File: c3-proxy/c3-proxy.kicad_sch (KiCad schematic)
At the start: 14 parts, among them J1 J-SAMTEC-TFM-120-X1-XXX-D-RA, J2 SFM-120-02-X-DH, J3 USB_C_Receptacle_USB2.0_16P, J4 Barrel_Jack, U9 IP4234CZ6,125

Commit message: style and logic fixes
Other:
- note added: "not sure the ideal way to connect/route this capacitor"
- moved on the sheet: HW1, HW2, HW3
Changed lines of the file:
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@@
 		)
 	)
+	(text "not sure the ideal way to connect/route this capacitor"
+		(exclude_from_sim no)
+		(at 53.848 244.856 0)
+		(effects
+			(font
+				(size 1.27 1.27)
+			)
+		)
+	)
 	(text "Outside Negitive\nInside Positive"
 		(exclude_from_sim no)
@@
 	)
 	(junction
+		(at 208.28 69.85)
+		(diameter 0)
+		(color 0 0 0 0)
+	)
+	(junction
 		(at 118.11 105.41)
 		(diameter 0)
@@
 	)
 	(junction
-		(at 208.28 69.85)
-		(diameter 0)
-		(color 0 0 0 0)
-	)
-	(junction
 		(at 118.11 82.55)
 		(diameter 0)
@@
 	(wire
 		(pts
-			(xy 208.28 69.85) (xy 118.11 69.85)
+			(xy 118.11 69.85) (xy 208.28 69.85)
 		)
 		(stroke
@@
 	(wire
 		(pts
-			(xy 208.28 69.85) (xy 208.28 154.94)
-		)
-		(stroke
-			(width 0)
-			(type default)
-		)
-	)
-	(wire
-		(pts
 			(xy 284.48 102.87) (xy 280.67 102.87)
 		)
@@
 	(wire
 		(pts
-			(xy 210.82 74.93) (xy 210.82 154.94)
-		)
-		(stroke
-			(width 0)
-			(type default)
-		)
-	)
-	(wire
-		(pts
 			(xy 284.48 80.01) (xy 118.11 80.01)
 		)
@@
 	(wire
 		(pts
+			(xy 208.28 69.85) (xy 284.48 69.85)
+		)
+		(stroke
+			(width 0)
+			(type default)
+		)
+	)
+	(wire
+		(pts
 			(xy 129.54 102.87) (xy 118.11 102.87)
 		)
@@
 	(wire
 		(pts
+			(xy 208.28 69.85) (xy 208.28 154.94)
+		)
+		(stroke
+			(width 0)
+			(type default)
+		)
+	)
+	(wire
+		(pts
 			(xy 288.29 110.49) (xy 284.48 110.49)
 		)
@@
 	(wire
 		(pts
-			(xy 288.29 54.61) (xy 114.3 54.61)
+			(xy 118.11 74.93) (xy 210.82 74.93)
 		)
 		(stroke
@@
 	(wire
 		(pts
-			(xy 288.29 52.07) (xy 114.3 52.07)
+			(xy 288.29 54.61) (xy 114.3 54.61)
 		)
 		(stroke
@@
 	(wire
 		(pts
-			(xy 83.82 194.31) (xy 88.9 194.31)
+			(xy 288.29 52.07) (xy 114.3 52.07)
 		)
 		(stroke
@@
 	(wire
 		(pts
-			(xy 118.11 77.47) (xy 118.11 80.01)
+			(xy 83.82 194.31) (xy 88.9 194.31)
 		)
 		(stroke
@@
 	(wire
 		(pts
-			(xy 223.52 130.81) (xy 114.3 130.81)
+			(xy 118.11 77.47) (xy 118.11 80.01)
 		)
 		(stroke
@@
 	(wire
 		(pts
-			(xy 273.05 100.33) (xy 273.05 97.79)
+			(xy 223.52 130.81) (xy 114.3 130.81)
 		)
 		(stroke
@@
 	(wire
 		(pts
-			(xy 288.29 74.93) (xy 284.48 74.93)
+			(xy 273.05 100.33) (xy 273.05 97.79)
 		)
 		(stroke
@@
 	(wire
 		(pts
-			(xy 210.82 74.93) (xy 118.11 74.93)
+			(xy 288.29 74.93) (xy 284.48 74.93)
 		)
 		(stroke
@@
 	(wire
 		(pts
-			(xy 284.48 74.93) (xy 210.82 74.93)
-		)
-		(stroke
-			(width 0)
-			(type default)
-		)
-	)
-	(wire
-		(pts
 			(xy 80.01 166.37) (xy 80.01 163.83)
 		)
@@
 	(wire
 		(pts
+			(xy 210.82 74.93) (xy 284.48 74.93)
+		)
+		(stroke
+			(width 0)
+			(type default)
+		)
+	)
+	(wire
+		(pts
 			(xy 288.29 77.47) (xy 284.48 77.47)
 		)
@@
 	(wire
 		(pts
-			(xy 284.48 69.85) (xy 208.28 69.85)
-		)
-		(stroke
-			(width 0)
-			(type default)
-		)
-	)
-	(wire
-		(pts
 			(xy 288.29 92.71) (xy 284.48 92.71)
 		)
@@
 	(wire
 		(pts
+			(xy 210.82 74.93) (xy 210.82 154.94)
+		)
+		(stroke
+			(width 0)
+			(type default)
+		)
+	)
+	(wire
+		(pts
 			(xy 118.11 107.95) (xy 118.11 110.49)
 		)
@@
 	(symbol
 		(lib_id "oresat_stuff:M1.6_Mounting_Hole")
-		(at 340.36 184.15 0)
+		(at 360.68 157.48 0)
 		(unit 1)
 		(body_style 1)
@@
 		(fields_autoplaced yes)
 		(property "Reference" "HW1"
-			(at 342.9 182.8799 0)
+			(at 363.22 156.2099 0)
 			(show_name no)
 			(do_not_autoplace no)
@@
 		)
 		(property "Value" "M1.6_Mounting_Hole"
-			(at 342.9 185.4199 0)
+			(at 363.22 158.7499 0)
 			(show_name no)
 			(do_not_autoplace no)
@@
 		)
 		(property "Footprint" "oresat-misc:M1.6 Mounting Hole"
-			(at 340.36 191.77 0)
+			(at 360.68 165.1 0)
 			(hide yes)
 			(show_name no)
@@
 		)
 		(property "Datasheet" ""
-			(at 340.36 184.15 0)
+			(at 360.68 157.48 0)
 			(hide yes)
 			(show_name no)
@@
 		)
 		(property "Description" ""
-			(at 340.36 184.15 0)
+			(at 360.68 157.48 0)
 			(hide yes)
 			(show_name no)
@@
 	(symbol
 		(lib_id "oresat_stuff:M1.6_Mounting_Hole")
-		(at 340.36 193.04 0)
+		(at 360.68 166.37 0)
 		(unit 1)
 		(body_style 1)
@@
 		(fields_autoplaced yes)
 		(property "Reference" "HW2"
-			(at 342.9 191.7699 0)
+			(at 363.22 165.0999 0)
 			(show_name no)
 			(do_not_autoplace no)
@@
 		)
 		(property "Value" "M1.6_Mounting_Hole"
-			(at 342.9 194.3099 0)
+			(at 363.22 167.6399 0)
 			(show_name no)
 			(do_not_autoplace no)
@@
 		)
 		(property "Footprint" "oresat-misc:M1.6 Mounting Hole"
-			(at 340.36 200.66 0)
+			(at 360.68 173.99 0)
 			(hide yes)
 			(show_name no)
@@
 		)
 		(property "Datasheet" ""
-			(at 340.36 193.04 0)
+			(at 360.68 166.37 0)
 			(hide yes)
 			(show_name no)
@@
 		)
 		(property "Description" ""
-			(at 340.36 193.04 0)
+			(at 360.68 166.37 0)
 			(hide yes)
 			(show_name no)
@@
 	(symbol
 		(lib_id "oresat_stuff:M1.6_Mounting_Hole")
-		(at 340.36 201.93 0)
+		(at 360.68 175.26 0)
 		(unit 1)
 		(body_style 1)
@@
 		(fields_autoplaced yes)
 		(property "Reference" "HW3"
-			(at 342.9 200.6599 0)
+			(at 363.22 173.9899 0)
 			(show_name no)
 			(do_not_autoplace no)
@@
 		)
 		(property "Value" "M1.6_Mounting_Hole"
-			(at 342.9 203.1999 0)
+			(at 363.22 176.5299 0)
 			(show_name no)
 			(do_not_autoplace no)
@@
 		)
 		(property "Footprint" "oresat-misc:M1.6 Mounting Hole"
-			(at 340.36 209.55 0)
+			(at 360.68 182.88 0)
 			(hide yes)
 			(show_name no)
@@
 		)
 		(property "Datasheet" ""
-			(at 340.36 201.93 0)
+			(at 360.68 175.26 0)
 			(hide yes)
 			(show_name no)
@@
 		)
 		(property "Description" ""
-			(at 340.36 201.93 0)
+			(at 360.68 175.26 0)
 			(hide yes)
 			(show_name no)
@@
 		)
 		(pin "OPD_SCL" input
-			(at 210.82 154.94 90)
+			(at 208.28 154.94 90)
 			(effects
 				(font
@@
 		)
 		(pin "OPD_PWR" input
-			(at 208.28 154.94 90)
+			(at 210.82 154.94 90)
 			(effects
 				(font

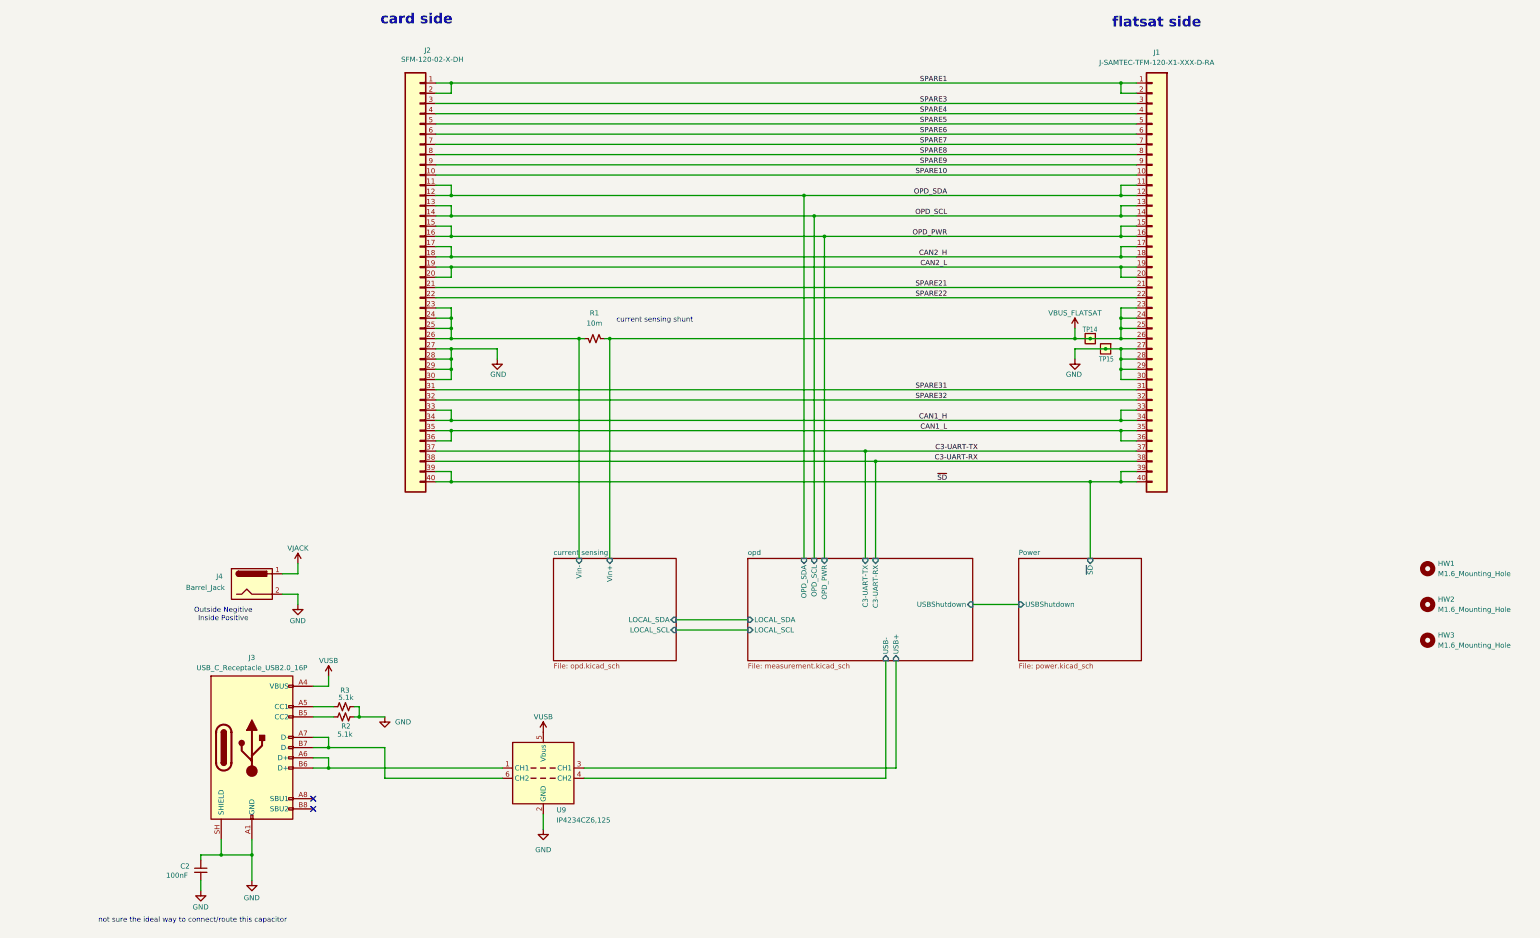
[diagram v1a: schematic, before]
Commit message: final layout and schematic touch ups
killed buzzer
deleted old folder
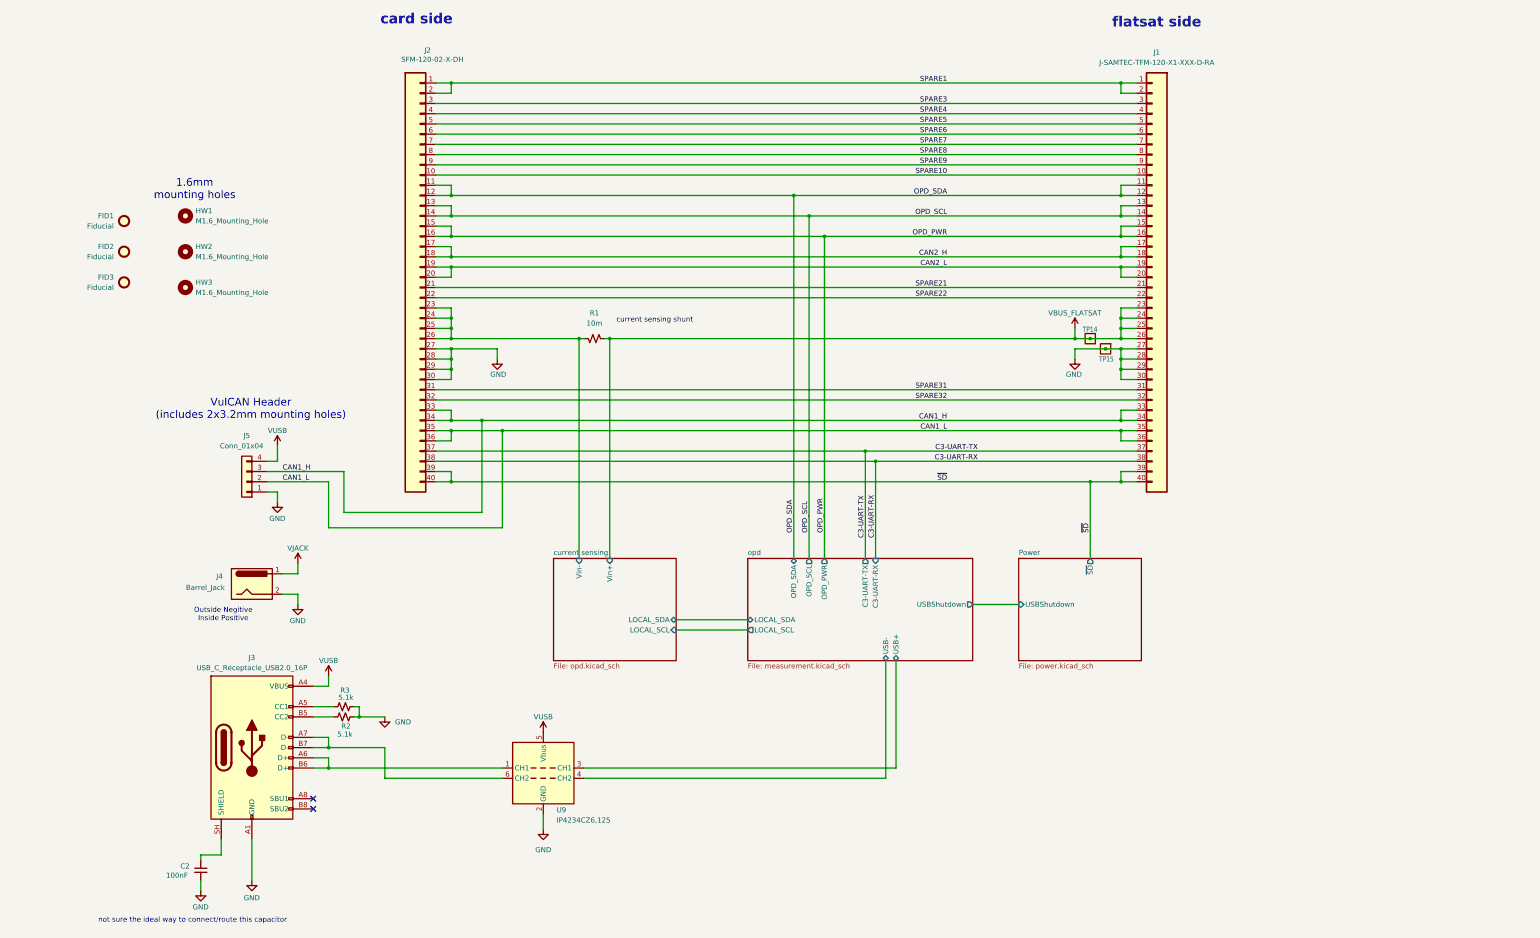
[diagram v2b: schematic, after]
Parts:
- added FID1, FID2, FID3: Fiducial, Fiducial:Fiducial_0.5mm_Mask1mm, symbol Mechanical:Fiducial
- added J5: Conn_01x04, Connector_PinHeader_2.54mm:PinHeader_1x04_P2.54mm_Vertical, symbol Connector_Generic:Conn_01x04
- C2: DIST (none) -> DigiKey; DPN (none) -> 399-6856-1-ND; MFR (none) -> KEMET; MPN (none) -> C0603C104K5RACAUTO
- J1: DIST (none) -> DigiKey; DPN (none) -> SAM10145-ND; MFR (none) -> Samtec Inc.; MPN (none) -> TFM-120-01-L-D-RA
- J2: DIST (none) -> DigiKey; DPN (none) -> SAM11706-ND; MFR (none) -> Samtec Inc.; MPN (none) -> SFM-120-01-S-D-LC
- J3: DIST (none) -> DigiKey; DPN (none) -> 2073-USB4105-GF-ACT-ND; MFR (none) -> GCT; MPN (none) -> USB4105-GF-A
- J4: DIST (none) -> DigiKey; DPN (none) -> CP-002A-ND; MFR (none) -> Category Connectors, Interconnects, Barrel Connectors, Powe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; MPN (none) -> PJ-002A
- R1: DIST (none) -> DigiKey; DPN (none) -> 696-1374-1-ND; MFR (none) -> Riedon; MPN (none) -> CSR1206-0R01F1
- R2, R3: DIST (none) -> DigiKey; DPN (none) -> RMCF0603FT5K10CT-ND; MFR (none) -> Stackpole Electronics; MPN (none) -> RMCF0603FT5K10
- U9: DIST (none) -> DigiKey
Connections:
- net CAN1_H: now also J5.3 (Pin_3)
- net CAN1_L: now also J5.2 (Pin_2)
- net GND: now also J5.1 (Pin_1); no longer C2.1, J3.SH (SHIELD)
- net VUSB: now also J5.4 (Pin_4)
- new net: C2.1, J3.SH (SHIELD)
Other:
- note added: "1.6mm mounting holes"
- note added: "VulCAN Header (includes 2x3.2mm mounting holes)"
- moved on the sheet: HW1, HW2, HW3

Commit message: restor changes again
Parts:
- R1: DPN 696-1374-1-ND -> WSLC-.01TR-ND; MFR Riedon -> Vishay Dale; MPN CSR1206-0R01F1 -> WSL1206R0100FEA
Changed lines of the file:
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@@
 			)
 		)
-		(property "Datasheet" "https://riedon.com/media/pdf/CSR.pdf"
+		(property "Datasheet" "https://www.vishay.com/docs/30100/wsl.pdf"
 			(at 153.67 100.33 0)
 			(hide yes)
@@
 			)
 		)
-		(property "Description" "10 mOhms ±1% 1W Chip Resistor 1206 (3216 Metric) Current Sense, Non-Inductive Metal Element"
+		(property "Description" "10 mOhms ±1% 0.25W, 1/4W Chip Resistor 1206 (3216 Metric) Anti-Sulfur, Automotive AEC-Q200, Current Sense, Moisture Resistant, Pulse Withstanding Metal Element"
 			(at 153.67 100.33 0)
 			(hide yes)
@@
 			)
 		)
-		(property "DPN" "696-1374-1-ND"
+		(property "DPN" "WSLC-.01TR-ND"
 			(at 153.67 100.33 90)
 			(hide yes)
@@
 			)
 		)
-		(property "MFR" "Riedon"
+		(property "MFR" "Vishay Dale"
 			(at 153.67 100.33 90)
 			(hide yes)
@@
 			)
 		)
-		(property "MPN" "CSR1206-0R01F1"
+		(property "MPN" "WSL1206R0100FEA"
 			(at 153.67 100.33 90)
 			(hide yes)

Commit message: Fix library paths and start fixing ERCs
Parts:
- TP14, TP15: symbol oresat_stuff:Test-Point-0.75mm-th -> oresat-misc:Test-Point-0.75mm-th
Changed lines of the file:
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@@
 	)
 	(symbol
-		(lib_id "oresat_stuff:VBUS")
+		(lib_id "power:VBUS")
 		(at 87.63 184.15 0)
 		(unit 1)
@@
 	)
 	(symbol
-		(lib_id "oresat_stuff:Test-Point-0.75mm-th")
+		(lib_id "oresat-misc:Test-Point-0.75mm-th")
 		(at 276.86 100.33 0)
 		(mirror y)
@@
 	)
 	(symbol
-		(lib_id "oresat_stuff:VBUS")
+		(lib_id "power:VBUS")
 		(at 80.01 156.21 0)
 		(unit 1)
@@
 	)
 	(symbol
-		(lib_id "oresat_stuff:VBUS")
+		(lib_id "power:VBUS")
 		(at 140.97 198.12 0)
 		(unit 1)
@@
 	)
 	(symbol
-		(lib_id "oresat_stuff:Test-Point-0.75mm-th")
+		(lib_id "oresat-misc:Test-Point-0.75mm-th")
 		(at 280.67 102.87 0)
 		(mirror y)
@@
 	)
 	(symbol
-		(lib_id "oresat_stuff:VBUS")
+		(lib_id "power:VBUS")
 		(at 74.93 127 0)
 		(unit 1)
@@
 	)
 	(symbol
-		(lib_id "oresat_stuff:VBUS")
+		(lib_id "power:VBUS")
 		(at 273.05 97.79 0)
 		(mirror y)

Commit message: did like... everything...
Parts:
- HW1, HW2, HW3: value M1.6_Mounting_Hole -> M3 mounting hole; footprint oresat-misc:M1.6 Mounting Hole -> MountingHole:MountingHole_3.2mm_M3; symbol oresat_stuff:M1.6_Mounting_Hole -> Mechanical:MountingHole
- J1: symbol oresat_stuff:J-SAMTEC-TFM-120-01-L-D-RA -> oresat-connectors:J-SAMTEC-TFM-120-01-L-D-RA
- J2: symbol oresat_stuff:J-SAMTEC-TFM-120-01-L-D-RA -> oresat-connectors:J-SAMTEC-SFM-120-X1-XXX-D
- J4: footprint Connector_BarrelJack:BarrelJack_CUI_PJ-102AH_Horizontal -> Connector_BarrelJack:BarrelJack_GCT_DCJ200-10-A_Horizontal; symbol Connector:Barrel_Jack -> Connector:Barrel_Jack_MountingPin; DPN CP-002A-ND -> 2073-DCJ200-10-A-K1-K-ND; MFR Category Connectors, Interconnects, Barrel Connectors, Powe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 -> GCT; MPN PJ-002A -> DCJ200-10-A-K1-K
- U9: symbol oresat_stuff:ip4234cz6 -> oresat-ics:ip4234cz6
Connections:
- net GND: now also J4.MP (MountPin)
- no-connect marks 2 -> 4

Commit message: v1.0 of the C3 Proxy sent off to fabrication.
Added makefile and README. Fixed a bunch of BOM issues, mostly just EOL and out of stock components. Fixed wrong footprints in the BOM, and switched diode from TH to SMT. Cleaned up some traces for funsies,
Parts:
- added TP16: Test-Point, oresat-misc:TestPoint-0.75mm-th, symbol oresat-misc:Test-Point-0.75mm-th
- C2: value 100nF -> 100n; footprint oresat-passives:0805-A -> oresat-passives:0603-A
- FID1, FID2, FID3: footprint Fiducial:Fiducial_0.5mm_Mask1mm -> Fiducial:Fiducial_1mm_Mask2mm
- J1: value J-SAMTEC-TFM-120-X1-XXX-D-RA -> TFM-120-X1-XXX-D-RA
- J2: value SFM-120-02-X-DH -> SFM-120-02-L-DH; symbol oresat-connectors:J-SAMTEC-SFM-120-X1-XXX-D -> Connector_Generic_MountingPin:Conn_01x40_MountingPin; DPN SAM11706-ND -> SAM14509CT-ND; MPN SFM-120-01-S-D-LC -> SFM-120-02-L-DH-TR
- J4: value Barrel_Jack -> DCJ200-10-A-K1-K; symbol Connector:Barrel_Jack_MountingPin -> Connector:Barrel_Jack_Switch
- R1: footprint oresat-passives:1206-B -> Resistor_SMD:R_1206_3216Metric; DPN WSLC-.01TR-ND -> 541-WSLP1206R0100DEACT-ND; MPN WSL1206R0100FEA -> WSLP1206R0100DEA
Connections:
- net GND: now also J2.MP (MountPin), J4.3; no longer J4.MP (MountPin)
- net VUSB: no longer J5.4 (Pin_4)
- new net: J5.4 (Pin_4), TP16.1
- no-connect marks 4 -> 2
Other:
- moved on the sheet: J4

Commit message: decreased size to fit in EU, transistor orientation
changed DC jack to be edge connected.
adjusted layout in top-right corner to still fit mounting hole.
fixed transistor orientation by switching to GSD symbols
moved SW2 and clarified silkscreen with boxes
changed via sizes to be standardized
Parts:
- removed J4: DCJ200-10-A-K1-K, Connector_BarrelJack:BarrelJack_GCT_DCJ200-10-A_Horizontal, symbol Connector:Barrel_Jack_Switch
- added J4: Barrel_Jack_Switch_MountingPin, oresat-connectors:SAMESKY_PJ-069B-SMT-TR, symbol Connector:Barrel_Jack_Switch_MountingPin
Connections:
- net GND: now also J4.2, J4.3
- net VJACK: now also J4.1
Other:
- note added: "Recommend these 90deg USB and DC JACK connectors for easier connections in EU USB-C M-F 90Degree connector https://www.amazon.com/gp/aw/d/B0CNGJTKNK/?th=1 DC Jack 5.5x2.1mm 90Degree M-F connector https://www.amazon.com/ZYAMY-5-5x2-1mm-Adapter-Charging-Connector/dp/B07YWQ118Y/ref=sr_1_9?th=1"
- title: Flatsat Interface Card -> c3-Proxy card
- moved on the sheet: C2, FID1, FID2, FID3, HW1, HW2, HW3, J1, J2, J3, J5, R1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
